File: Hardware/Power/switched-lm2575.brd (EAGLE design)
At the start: 38.1 x 25.4 mm, 8 parts

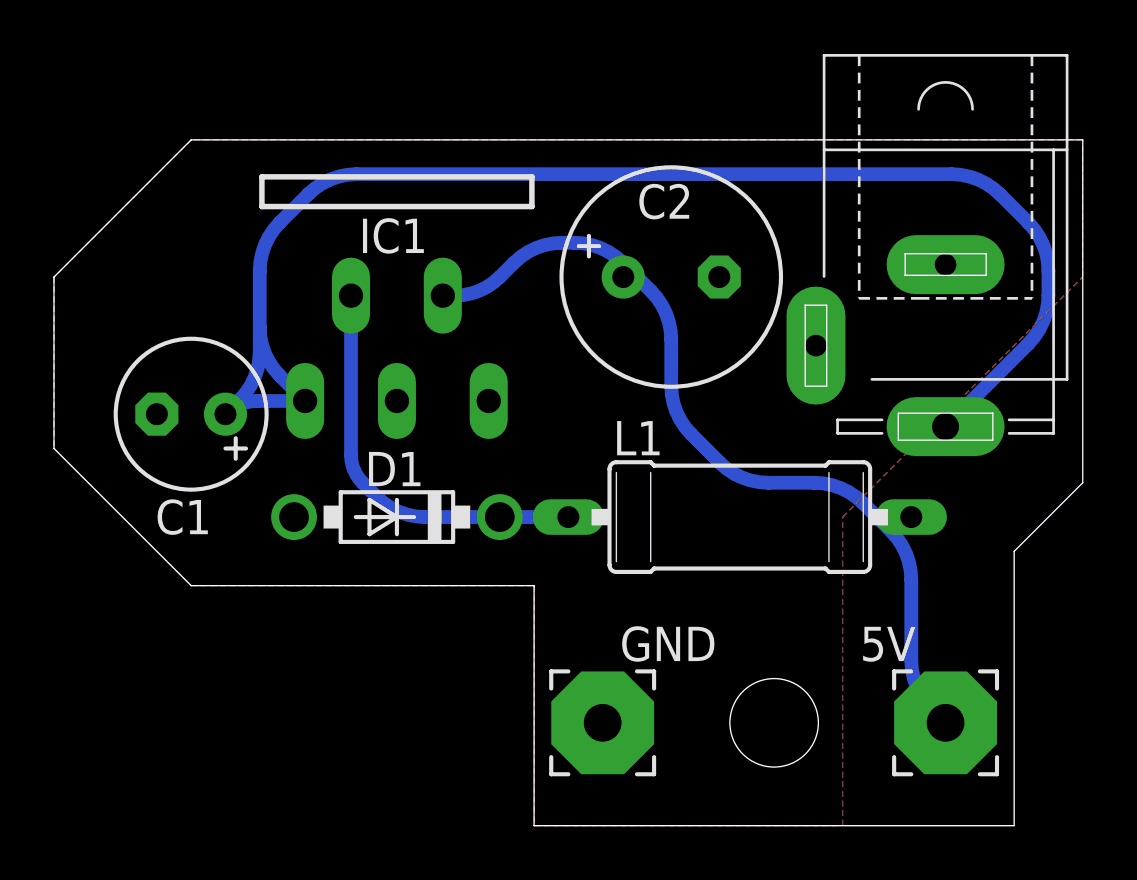
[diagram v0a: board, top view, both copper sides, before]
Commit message: Updates to combined board inc. new blitter features
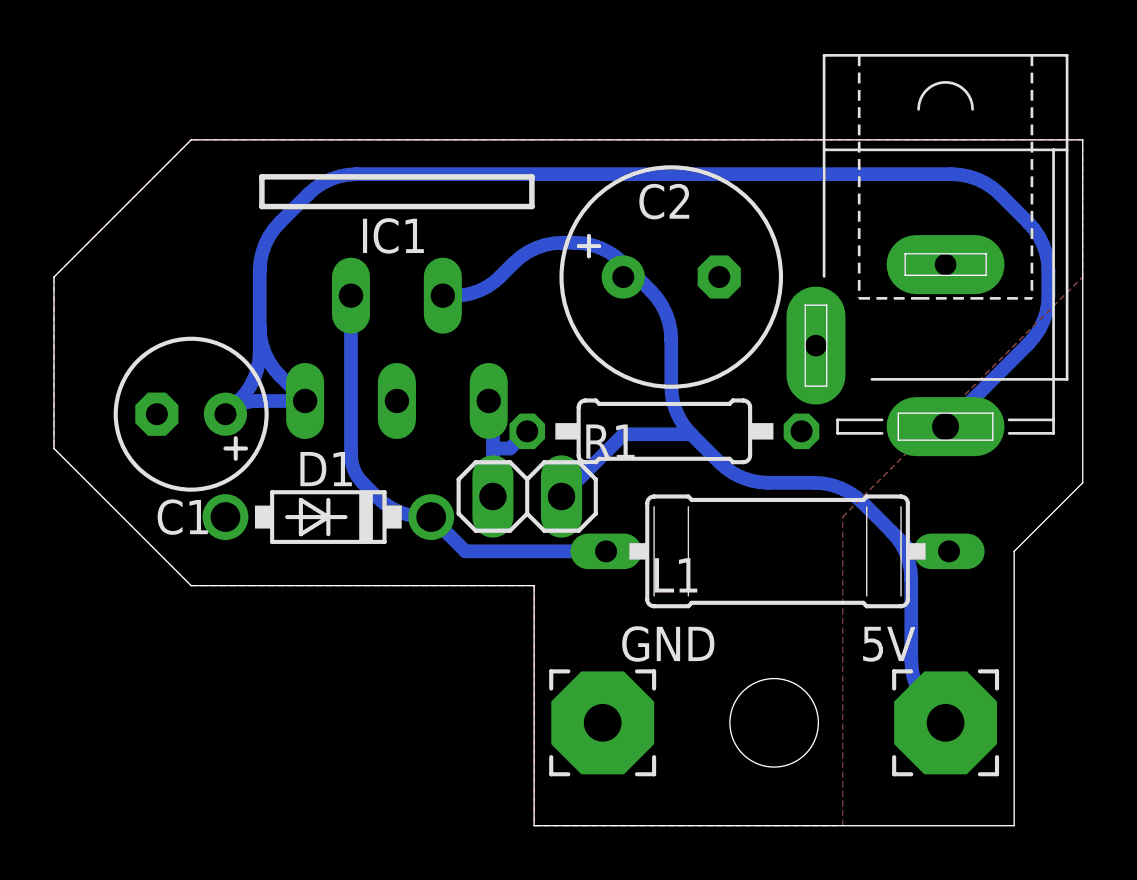
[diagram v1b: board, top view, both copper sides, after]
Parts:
- added JP1: (no value), pinhead:1X02
- added R1: (no value), rcl:0207/10
- moved D1 2.54 mm to (-10.2, 11.4)
- moved L1 1.89 mm to (6.48, 10.2)
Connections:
- new net N$3: IC1.5, JP1.1, R1.1
- net GND: now also R1.2; no longer IC1.5
- net VCC: now also JP1.2
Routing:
- net VCC: track 32.4 -> 39.3 mm
- net N$3: track 0.00 -> 5.14 mm
- net N$2: track 15.0 -> 16.9 mm
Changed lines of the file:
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@@
 </layers>
 <board>
-<fusionsync huburn="a.cGVyc29uYWw6dWUyYWI4Y2Y5" projecturn="a.cGVyc29uYWw6dWUyYWI4Y2Y5IzIwMTgxMTEyMTU5Njk3ODMx" f3durn="urn:adsk.wipprod:dm.lineage:c6tb-7JRRiK4hgRljbvFAA" pcbguid="ef877cea-3dd2-439d-9d2a-7c6b6e2ee77c" lastpulledtime="" lastsyncedchangeguid="" latestrevisionid="80c4534b-8843-4731-9d04-19d34fab2bae" lastsyncedrevisionid="80c4534b-8843-4731-9d04-19d34fab2bae" lastboardhashguid="9329cf81-843c-0b8c-f49d-f8f2b09a7f85" lastpushedtime="2021-06-22T23:16:55Z" linktopcb3d="true"/>
+<fusionsync huburn="a.cGVyc29uYWw6dWUyYWI4Y2Y5" projecturn="a.cGVyc29uYWw6dWUyYWI4Y2Y5IzIwMTgxMTEyMTU5Njk3ODMx" f3durn="urn:adsk.wipprod:dm.lineage:c6tb-7JRRiK4hgRljbvFAA" pcbguid="" lastpulledtime="" lastsyncedchangeguid="" latestrevisionid="80c4534b-8843-4731-9d04-19d34fab2bae" lastsyncedrevisionid="80c4534b-8843-4731-9d04-19d34fab2bae" lastboardhashguid="9329cf81-843c-0b8c-f49d-f8f2b09a7f85" lastpushedtime="2021-06-22T23:16:55Z" linktopcb3d="true"/>
 <plain>
 <wire x1="-2.54" y1="0" x2="15.24" y2="0" width="0" layer="20"/>
@@
 <attribute name="VALUE" x="0.254" y="17.272" size="1.27" layer="27" ratio="10"/>
 </element>
-<element name="D1" library="diode" library_urn="urn:adsk.eagle:library:210" package="DO41-7.6" package3d_urn="urn:adsk.eagle:package:43421/1" override_package3d_urn="urn:adsk.eagle:package:29523036/2" override_package_urn="urn:adsk.eagle:footprint:43217/1" value="1N5819-B" x="-7.62" y="11.43" smashed="yes" rot="R180">
-<attribute name="NAME" x="-6.604" y="13.843" size="1.27" layer="25" ratio="10" rot="R180"/>
-<attribute name="POPULARITY" value="11" x="-38.1" y="29.21" size="1.778" layer="27" rot="R180" display="off"/>
-<attribute name="VALUE" x="-3.302" y="10.287" size="1.27" layer="27" ratio="10" rot="R180"/>
+<element name="D1" library="diode" library_urn="urn:adsk.eagle:library:210" package="DO41-7.6" package3d_urn="urn:adsk.eagle:package:43421/1" override_package3d_urn="urn:adsk.eagle:package:29523036/2" override_package_urn="urn:adsk.eagle:footprint:43217/1" value="1N5819-B" x="-10.16" y="11.43" smashed="yes" rot="R180">
+<attribute name="NAME" x="-9.144" y="13.843" size="1.27" layer="25" ratio="10" rot="R180"/>
+<attribute name="POPULARITY" value="11" x="-40.64" y="29.21" size="1.778" layer="27" rot="R180" display="off"/>
+<attribute name="VALUE" x="-5.842" y="10.287" size="1.27" layer="27" ratio="10" rot="R180"/>
 </element>
 <element name="IC1" library="linear" library_urn="urn:adsk.eagle:library:262" package="TO220-51" package3d_urn="urn:adsk.eagle:package:16439/1" override_package3d_urn="urn:adsk.eagle:package:29523014/2" override_package_urn="urn:adsk.eagle:footprint:16237/1" value="" x="-7.62" y="24.13" smashed="yes">
@@
 <attribute name="VALUE" x="6.35" y="27.94" size="1.27" layer="27" rot="R270"/>
 </element>
-<element name="L1" library="inductors" library_urn="urn:adsk.eagle:library:243" package="SMCC12" package3d_urn="urn:adsk.eagle:package:15103/1" override_package3d_urn="urn:adsk.eagle:package:29523025/2" override_package_urn="urn:adsk.eagle:footprint:15007/1" value="470uH" x="5.08" y="11.43" smashed="yes">
-<attribute name="NAME" x="0.381" y="13.716" size="1.27" layer="25" ratio="10"/>
-<attribute name="POPULARITY" value="0" x="38.1" y="-13.97" size="1.778" layer="27" display="off"/>
-<attribute name="SPICEPREFIX" value="L" x="38.1" y="-13.97" size="1.778" layer="27" display="off"/>
-<attribute name="VALUE" x="2.159" y="10.9982" size="1.27" layer="27" ratio="10"/>
+<element name="L1" library="inductors" library_urn="urn:adsk.eagle:library:243" package="SMCC12" package3d_urn="urn:adsk.eagle:package:15103/1" override_package3d_urn="urn:adsk.eagle:package:29523025/2" override_package_urn="urn:adsk.eagle:footprint:15007/1" value="470uH" x="6.477" y="10.16" smashed="yes">
+<attribute name="NAME" x="1.778" y="8.636" size="1.27" layer="25" ratio="10"/>
+<attribute name="POPULARITY" value="0" x="39.497" y="-15.24" size="1.778" layer="27" display="off"/>
+<attribute name="SPICEPREFIX" value="L" x="39.497" y="-15.24" size="1.778" layer="27" display="off"/>
+<attribute name="VALUE" x="4.826" y="9.7282" size="1.27" layer="27" ratio="10"/>
 </element>
 <element name="GND" library="wirepad" library_urn="urn:adsk.eagle:library:412" package="3,81/1,4" package3d_urn="urn:adsk.eagle:package:30835/1" value="" x="0" y="3.81" smashed="yes">
@@
 <attribute name="POPULARITY" value="14" x="35.56" y="-29.21" size="1.778" layer="27" display="off"/>
 <attribute name="VALUE" x="12.7" y="5.01" size="0.0254" layer="27"/>
+</element>
+<element name="JP1" library="pinhead" library_urn="urn:adsk.eagle:library:325" package="1X02" package3d_urn="urn:adsk.eagle:package:22435/2" value="" x="-2.794" y="12.192" smashed="yes">
+<attribute name="POPULARITY" value="98" x="-2.794" y="12.192" size="1.778" layer="27" display="off"/>
+<attribute name="VALUE" x="-5.334" y="9.017" size="1.27" layer="27"/>
+</element>
+<element name="R1" library="rcl" library_urn="urn:adsk.eagle:library:334" package="0207/10" package3d_urn="urn:adsk.eagle:package:23491/2" value="" x="2.286" y="14.605" smashed="yes">
+<attribute name="NAME" x="-0.762" y="13.589" size="1.27" layer="25" ratio="10"/>
+<attribute name="POPULARITY" value="36" x="2.286" y="14.605" size="1.778" layer="27" display="off"/>
+<attribute name="SPICEPREFIX" value="R" x="2.286" y="14.605" size="1.778" layer="27" display="off"/>
+<attribute name="VALUE" x="0.0254" y="13.97" size="1.27" layer="27" ratio="10"/>
 </element>
 </elements>
@@
 <wire x1="11.43" y1="6.132103125" x2="12.17395" y2="4.33605" width="0.508" layer="16" curve="45"/>
 <wire x1="12.17395" y1="4.33605" x2="12.7" y2="3.81" width="0.508" layer="16"/>
-<wire x1="9.63395" y1="11.95605" x2="10.16" y2="11.43" width="0.508" layer="16"/>
-<wire x1="10.16" y1="11.43" x2="10.68605" y2="10.90395" width="0.508" layer="16"/>
+<wire x1="9.63395" y1="11.95605" x2="10.68605" y2="10.90395" width="0.508" layer="16"/>
 <wire x1="11.43" y1="9.107896875" x2="11.43" y2="6.132103125" width="0.508" layer="16"/>
-<wire x1="11.43" y1="11.43" x2="10.16" y2="11.43" width="0.508" layer="16"/>
+<contactref element="JP1" pad="2"/>
+<wire x1="12.827" y1="10.16" x2="11.43" y2="10.16" width="0.508" layer="16"/>
+<wire x1="11.43" y1="10.16" x2="10.68605" y2="10.90395" width="0.508" layer="16"/>
+<wire x1="-1.524" y1="12.192" x2="0.78005" y2="14.49605" width="0.508" layer="16"/>
+<wire x1="0.78005" y1="14.49605" x2="3.28395" y2="14.49605" width="0.508" layer="16"/>
 </signal>
 <signal name="GND">
@@
 <contactref element="IC1" pad="3"/>
 <contactref element="C1" pad="-"/>
-<contactref element="IC1" pad="5"/>
 <contactref element="C2" pad="-"/>
 <polygon width="0.508" layer="1">
@@
 <vertex x="-15.24" y="8.89"/>
 </polygon>
+<contactref element="R1" pad="2"/>
 </signal>
 <signal name="VIN">
@@
 <wire x1="-8.89" y1="12.7" x2="-8.36395" y2="12.17395" width="0.508" layer="16"/>
 <wire x1="-8.36395" y1="12.17395" x2="-6.567896875" y2="11.43" width="0.508" layer="16" curve="45"/>
-<wire x1="-6.567896875" y1="11.43" x2="-3.81" y2="11.43" width="0.508" layer="16"/>
-<wire x1="-3.81" y1="11.43" x2="-1.27" y2="11.43" width="0.508" layer="16"/>
+<wire x1="-6.567896875" y1="11.43" x2="-6.35" y2="11.43" width="0.508" layer="16"/>
+<wire x1="-6.35" y1="11.43" x2="-5.08" y2="10.16" width="0.508" layer="16"/>
+<wire x1="0.127" y1="10.16" x2="-5.08" y2="10.16" width="0.508" layer="16"/>
+</signal>
+<signal name="N$3">
+<contactref element="JP1" pad="1"/>
+<contactref element="R1" pad="1"/>
+<contactref element="IC1" pad="5"/>
+<wire x1="-4.064" y1="12.192" x2="-4.064" y2="13.97" width="0.508" layer="16"/>
+<wire x1="-4.064" y1="13.97" x2="-4.064" y2="15.574" width="0.508" layer="16"/>
+<wire x1="-4.064" y1="15.574" x2="-4.22" y2="15.73" width="0.508" layer="16"/>
+<wire x1="-2.794" y1="14.605" x2="-3.429" y2="13.97" width="0.508" layer="16"/>
+<wire x1="-3.429" y1="13.97" x2="-4.064" y2="13.97" width="0.508" layer="16"/>
 </signal>
 </signals>
@@
 <mfgpreviewcolor name="substratecolor" color="0xFF786E46"/>
 </mfgpreviewcolors>
+<errors>
+</errors>
 </board>
 </drawing>

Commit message: RTC flash and power supply update
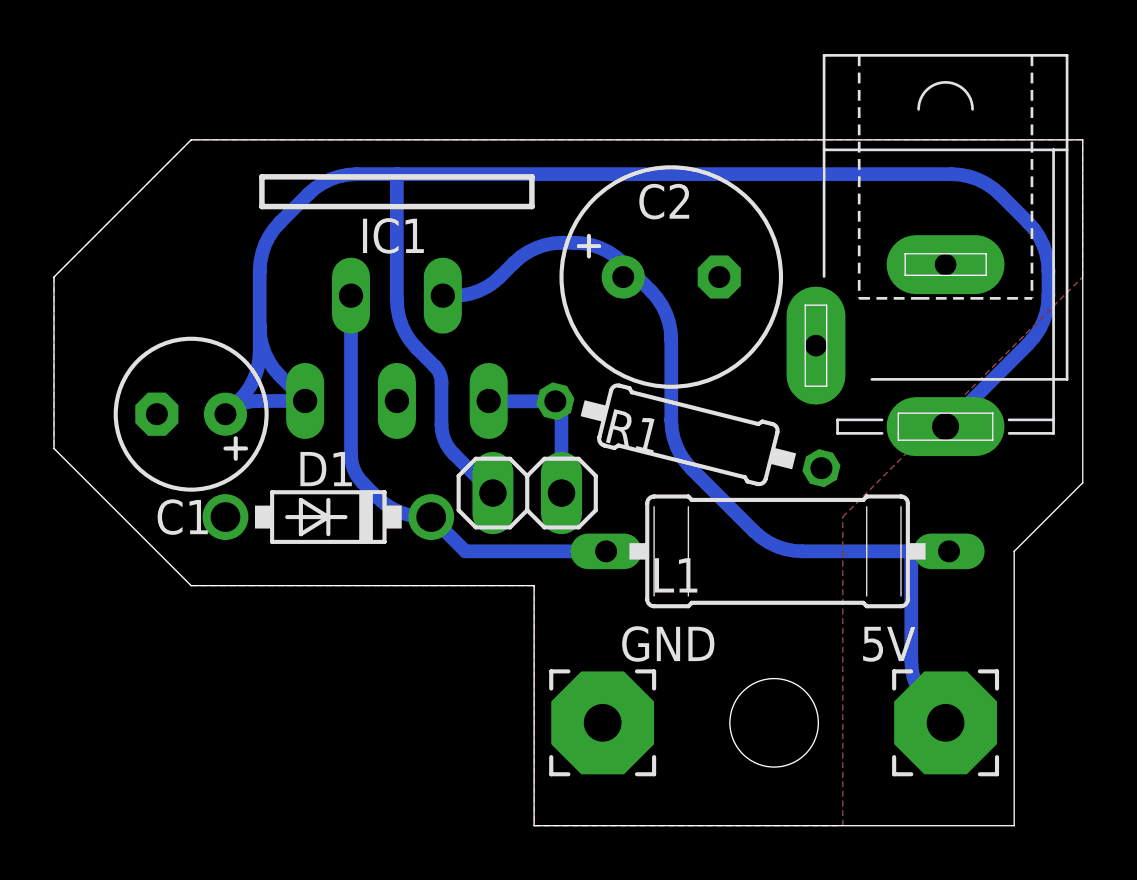
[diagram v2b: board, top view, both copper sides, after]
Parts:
- moved R1 0.90 mm to (3.17, 14.5), turned to 345.9 degrees
- moved JP1 0.13 mm to (-2.79, 12.3), turned to 180 degrees
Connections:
- net VCC: no longer JP1.2
- net VIN: now also JP1.2
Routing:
- net VIN: track 51.9 -> 64.9 mm
- net VCC: track 39.3 -> 33.5 mm
- net N$3: track 5.14 -> 5.97 mm
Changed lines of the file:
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@@
 <attribute name="VALUE" x="12.7" y="5.01" size="0.0254" layer="27"/>
 </element>
-<element name="JP1" library="pinhead" library_urn="urn:adsk.eagle:library:325" package="1X02" package3d_urn="urn:adsk.eagle:package:22435/2" value="" x="-2.794" y="12.192" smashed="yes">
-<attribute name="POPULARITY" value="98" x="-2.794" y="12.192" size="1.778" layer="27" display="off"/>
-<attribute name="VALUE" x="-5.334" y="9.017" size="1.27" layer="27"/>
+<element name="JP1" library="pinhead" library_urn="urn:adsk.eagle:library:325" package="1X02" package3d_urn="urn:adsk.eagle:package:22435/2" value="" x="-2.794" y="12.319" smashed="yes" rot="R180">
+<attribute name="POPULARITY" value="98" x="-2.794" y="12.319" size="1.778" layer="27" rot="R180" display="off"/>
+<attribute name="VALUE" x="-0.254" y="15.494" size="1.27" layer="27" rot="R180"/>
 </element>
-<element name="R1" library="rcl" library_urn="urn:adsk.eagle:library:334" package="0207/10" package3d_urn="urn:adsk.eagle:package:23491/2" value="" x="2.286" y="14.605" smashed="yes">
-<attribute name="NAME" x="-0.762" y="13.589" size="1.27" layer="25" ratio="10"/>
-<attribute name="POPULARITY" value="36" x="2.286" y="14.605" size="1.778" layer="27" display="off"/>
-<attribute name="SPICEPREFIX" value="R" x="2.286" y="14.605" size="1.778" layer="27" display="off"/>
-<attribute name="VALUE" x="0.0254" y="13.97" size="1.27" layer="27" ratio="10"/>
+<element name="R1" library="rcl" library_urn="urn:adsk.eagle:library:334" package="0207/10" package3d_urn="urn:adsk.eagle:package:23491/2" value="" x="3.175" y="14.478" smashed="yes" rot="R345.9">
+<attribute name="NAME" x="-0.02868125" y="14.235146875" size="1.27" layer="25" ratio="10" rot="R345.9"/>
+<attribute name="POPULARITY" value="36" x="3.175" y="14.478" size="1.778" layer="27" rot="R345.9" display="off"/>
+<attribute name="SPICEPREFIX" value="R" x="3.175" y="14.478" size="1.778" layer="27" rot="R345.9" display="off"/>
+<attribute name="VALUE" x="0.827809375" y="14.412846875" size="1.27" layer="27" ratio="10" rot="R345.9"/>
 </element>
 </elements>
@@
 <contactref element="C2" pad="+"/>
 <contactref element="L1" pad="2"/>
-<wire x1="4.33605" y1="13.44395" x2="6.132103125" y2="12.7" width="0.508" layer="16" curve="45"/>
-<wire x1="4.33605" y1="13.44395" x2="3.28395" y2="14.49605" width="0.508" layer="16"/>
-<wire x1="3.28395" y1="14.49605" x2="2.54" y2="16.292103125" width="0.508" layer="16" curve="-45"/>
 <wire x1="1.79605" y1="19.79395" x2="2.54" y2="17.997896875" width="0.508" layer="16" curve="-45"/>
-<wire x1="2.54" y1="16.292103125" x2="2.54" y2="17.997896875" width="0.508" layer="16"/>
 <wire x1="-5.92" y1="19.63" x2="-5.47580625" y2="19.63" width="0.508" layer="16"/>
 <wire x1="-5.47580625" y1="19.63" x2="-3.81" y2="20.32" width="0.508" layer="16" curve="45"/>
@@
 <wire x1="1.27" y1="20.32" x2="1.79605" y2="19.79395" width="0.508" layer="16"/>
 <wire x1="0.762" y1="20.32" x2="1.27" y2="20.32" width="0.508" layer="16"/>
-<wire x1="6.132103125" y1="12.7" x2="7.837896875" y2="12.7" width="0.508" layer="16"/>
-<wire x1="7.837896875" y1="12.7" x2="9.63395" y2="11.95605" width="0.508" layer="16" curve="-45"/>
-<wire x1="10.68605" y1="10.90395" x2="11.43" y2="9.107896875" width="0.508" layer="16" curve="-45"/>
-<wire x1="11.43" y1="6.132103125" x2="12.17395" y2="4.33605" width="0.508" layer="16" curve="45"/>
+<wire x1="12.17395" y1="4.33605" x2="11.43" y2="6.132103125" width="0.508" layer="16" curve="-45"/>
 <wire x1="12.17395" y1="4.33605" x2="12.7" y2="3.81" width="0.508" layer="16"/>
-<wire x1="9.63395" y1="11.95605" x2="10.68605" y2="10.90395" width="0.508" layer="16"/>
-<wire x1="11.43" y1="9.107896875" x2="11.43" y2="6.132103125" width="0.508" layer="16"/>
-<contactref element="JP1" pad="2"/>
-<wire x1="12.827" y1="10.16" x2="11.43" y2="10.16" width="0.508" layer="16"/>
-<wire x1="11.43" y1="10.16" x2="10.68605" y2="10.90395" width="0.508" layer="16"/>
-<wire x1="-1.524" y1="12.192" x2="0.78005" y2="14.49605" width="0.508" layer="16"/>
-<wire x1="0.78005" y1="14.49605" x2="3.28395" y2="14.49605" width="0.508" layer="16"/>
+<wire x1="11.43" y1="10.16" x2="12.827" y2="10.16" width="0.508" layer="16"/>
+<wire x1="11.43" y1="6.132103125" x2="11.43" y2="10.16" width="0.508" layer="16"/>
+<wire x1="2.54" y1="15.022103125" x2="3.28395" y2="13.22605" width="0.508" layer="16" curve="45"/>
+<wire x1="5.60605" y1="10.90395" x2="7.402103125" y2="10.16" width="0.508" layer="16" curve="45"/>
+<wire x1="7.402103125" y1="10.16" x2="11.43" y2="10.16" width="0.508" layer="16"/>
+<wire x1="2.54" y1="17.997896875" x2="2.54" y2="15.022103125" width="0.508" layer="16"/>
+<wire x1="3.28395" y1="13.22605" x2="5.60605" y2="10.90395" width="0.508" layer="16"/>
 </signal>
 <signal name="GND">
@@
 <wire x1="-12.7" y1="18.462103125" x2="-11.95605" y2="16.66605" width="0.508" layer="16" curve="45"/>
 <wire x1="-11.95605" y1="16.66605" x2="-11.02" y2="15.73" width="0.508" layer="16"/>
-<wire x1="12.917896875" y1="24.13" x2="-9.107896875" y2="24.13" width="0.508" layer="16"/>
+<wire x1="12.917896875" y1="24.13" x2="-7.62" y2="24.13" width="0.508" layer="16"/>
+<wire x1="-7.62" y1="24.13" x2="-9.107896875" y2="24.13" width="0.508" layer="16"/>
 <wire x1="-10.90395" y1="23.38605" x2="-11.95605" y2="22.33395" width="0.508" layer="16"/>
 <wire x1="-12.7" y1="20.537896875" x2="-12.7" y2="18.462103125" width="0.508" layer="16"/>
@@
 <wire x1="-13.97" y1="15.24" x2="-12.787034375" y2="15.73" width="0.508" layer="16" curve="-45"/>
 <wire x1="-12.787034375" y1="15.73" x2="-11.02" y2="15.73" width="0.508" layer="16"/>
+<contactref element="JP1" pad="2"/>
+<wire x1="-4.064" y1="12.319" x2="-5.5199875" y2="13.7749875" width="0.508" layer="16"/>
+<wire x1="-5.5199875" y1="13.7749875" x2="-5.969" y2="14.859" width="0.508" layer="16" curve="-45"/>
+<wire x1="-5.969" y1="14.859" x2="-5.969" y2="16.404790625" width="0.508" layer="16"/>
+<wire x1="-6.223" y1="17.018" x2="-5.969" y2="16.404790625" width="0.508" layer="16" curve="-45"/>
+<wire x1="-7.62" y1="24.13" x2="-7.62" y2="19.467103125" width="0.508" layer="16"/>
+<wire x1="-7.62" y1="19.467103125" x2="-6.87605" y2="17.67105" width="0.508" layer="16" curve="45"/>
+<wire x1="-6.87605" y1="17.67105" x2="-6.223" y2="17.018" width="0.508" layer="16"/>
 </signal>
 <signal name="N$2">
@@
 <contactref element="R1" pad="1"/>
 <contactref element="IC1" pad="5"/>
-<wire x1="-4.064" y1="12.192" x2="-4.064" y2="13.97" width="0.508" layer="16"/>
-<wire x1="-4.064" y1="13.97" x2="-4.064" y2="15.574" width="0.508" layer="16"/>
-<wire x1="-4.064" y1="15.574" x2="-4.22" y2="15.73" width="0.508" layer="16"/>
-<wire x1="-2.794" y1="14.605" x2="-3.429" y2="13.97" width="0.508" layer="16"/>
-<wire x1="-3.429" y1="13.97" x2="-4.064" y2="13.97" width="0.508" layer="16"/>
+<wire x1="-4.22" y1="15.73" x2="-4.2055625" y2="15.7155625" width="0.508" layer="16"/>
+<wire x1="-4.2055625" y1="15.7155625" x2="-1.751946875" y2="15.7155625" width="0.508" layer="16"/>
+<wire x1="-1.751946875" y1="15.7155625" x2="-1.524" y2="15.487615625" width="0.508" layer="16"/>
+<wire x1="-1.524" y1="15.487615625" x2="-1.524" y2="12.319" width="0.508" layer="16"/>
 </signal>
 </signals>
